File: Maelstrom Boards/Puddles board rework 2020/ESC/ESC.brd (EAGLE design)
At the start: 101.6 x 101.6 mm, 63 parts, among them P5 MALE1PINHEADER, P6 MALE1PINHEADER, P7 MALE1PINHEADER, P8 MALE1PINHEADER

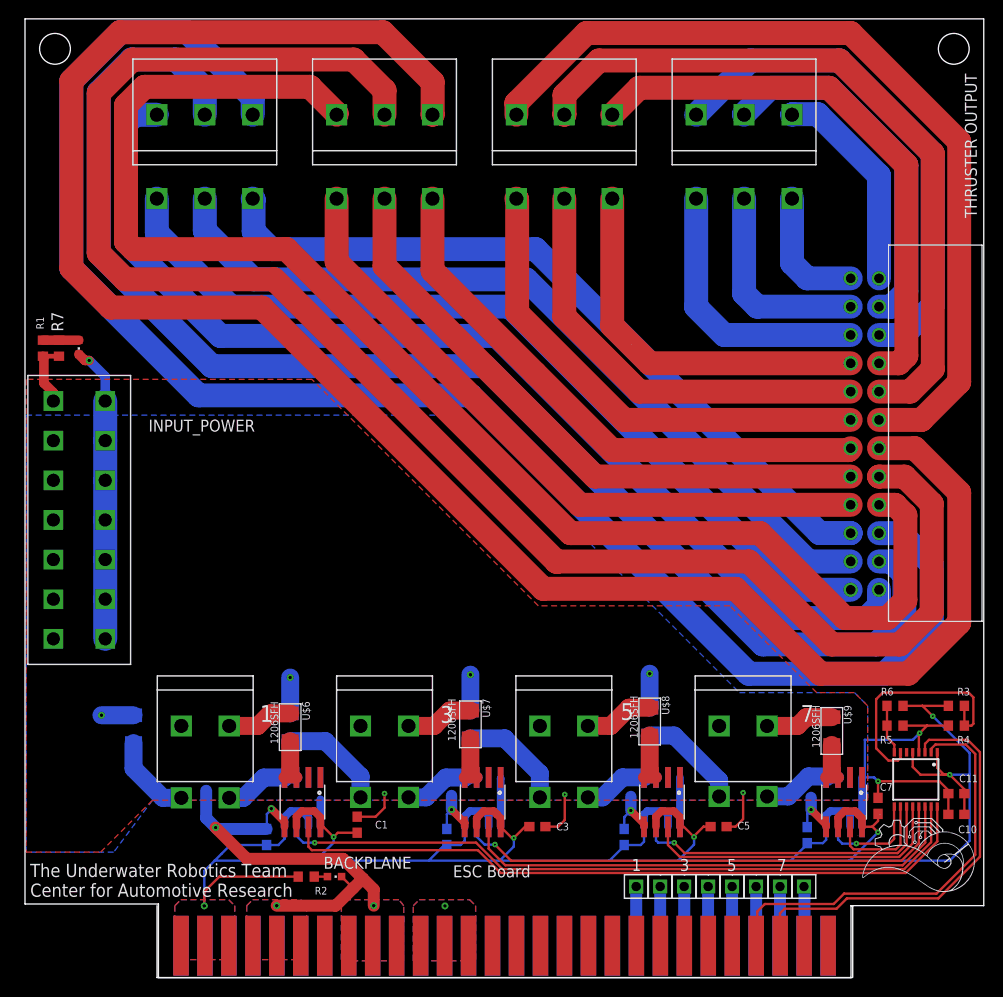
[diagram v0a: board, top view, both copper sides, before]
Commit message: updated puddles board rework ESC and Copro finished
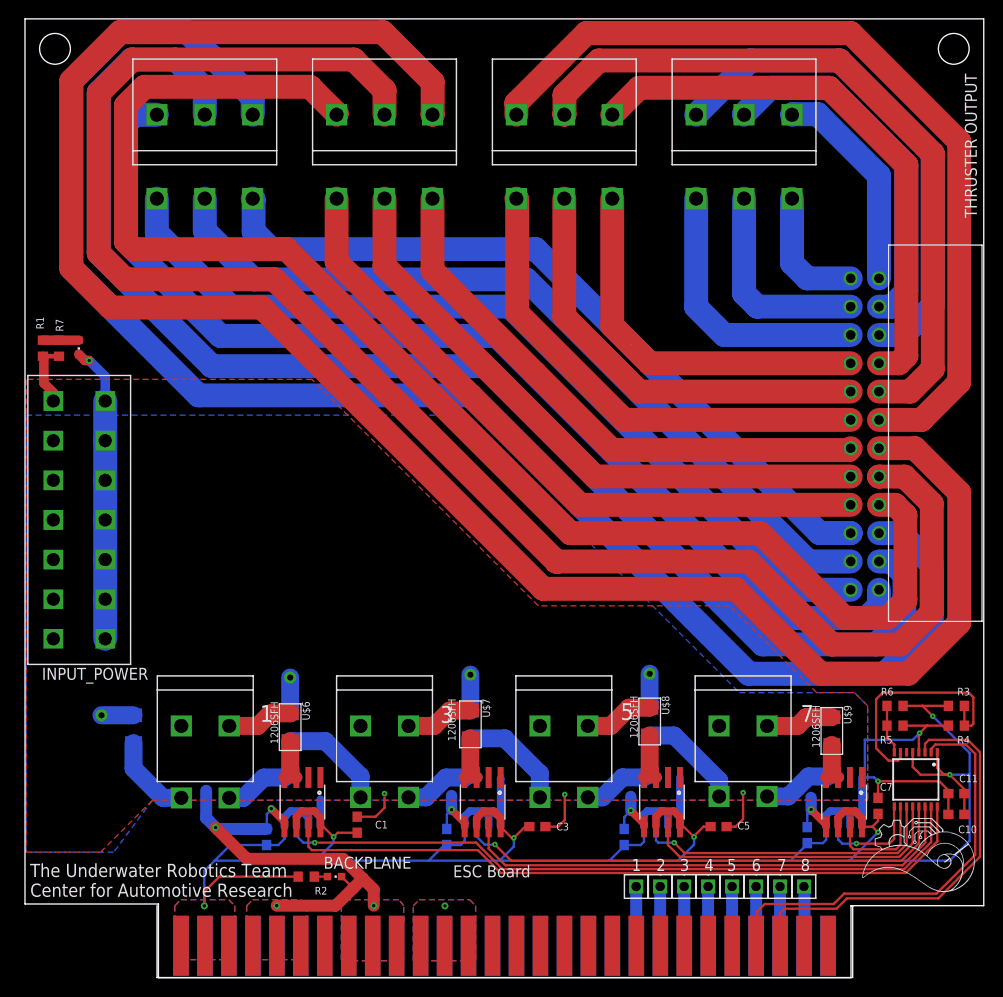
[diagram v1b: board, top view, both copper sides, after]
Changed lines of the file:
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@@
 <text x="2" y="68.7" size="0.8128" layer="25" rot="R90">R1</text>
 <text x="83.2" y="11.3" size="1.27" layer="26" rot="MR0">8</text>
+<text x="66.9" y="11.3" size="1.27" layer="25">2</text>
+<text x="72" y="11.3" size="1.27" layer="25">4</text>
+<text x="77" y="11.3" size="1.27" layer="25">6</text>
+<text x="82.2" y="11.3" size="1.27" layer="25">8</text>
+<text x="65.3" y="11.3" size="1.27" layer="26" rot="MR0">1</text>
+<text x="70.4" y="11.3" size="1.27" layer="26" rot="MR0">3</text>
+<text x="75.4" y="11.3" size="1.27" layer="26" rot="MR0">5</text>
+<text x="80.4" y="11.3" size="1.27" layer="26" rot="MR0">7</text>
 </plain>
 <attributes>
@@
 </element>
 <element name="INPUT_POWER" library="led" library_urn="urn:adsk.eagle:library:259" package="CHIPLED_0603" package3d_urn="urn:adsk.eagle:package:15822/2" value="" x="5.7" y="66.8" smashed="yes" rot="R180">
-<attribute name="NAME" x="24.365" y="59.13" size="1.27" layer="25" rot="R180"/>
+<attribute name="NAME" x="13.065" y="32.83" size="1.27" layer="25" rot="R180"/>
 <attribute name="VALUE" x="3.795" y="68.07" size="1.27" layer="27" rot="R270"/>
 </element>
@@
 </element>
 <element name="R7" library="resistor" library_urn="urn:adsk.eagle:library:348" package="R0603" package3d_urn="urn:adsk.eagle:package:26057/1" value="900" x="3.6" y="66.7" smashed="yes" rot="R90">
-<attribute name="NAME" x="4.065" y="68.465" size="1.27" layer="25" rot="R90"/>
+<attribute name="NAME" x="4.065" y="68.465" size="0.8128" layer="25" rot="R90"/>
 <attribute name="VALUE" x="5.505" y="66.065" size="1.27" layer="27" rot="R90"/>
 </element>
@@
 <contactref element="U$3" pad="P$1"/>
 <wire x1="11.5" y1="27.8" x2="8.1" y2="27.8" width="1.905" layer="16"/>
-<via x="8.1" y="27.8" extent="1-16" drill="0.35"/>
+<via x="8.1" y="27.8" extent="1-16" drill="0.65" diameter="1.3"/>
 <wire x1="28.1" y1="28" x2="28.1" y2="31.8" width="1.905" layer="16"/>
-<via x="28.1" y="31.8" extent="1-16" drill="0.35"/>
+<via x="28.1" y="31.8" extent="1-16" drill="0.65" diameter="1.3"/>
 <wire x1="47.2" y1="28.3" x2="47.2" y2="32.1" width="1.905" layer="16"/>
-<via x="47.2" y="32.1" extent="1-16" drill="0.35"/>
+<via x="47.2" y="32.1" extent="1-16" drill="0.65" diameter="1.3"/>
 <wire x1="66.2" y1="28.6" x2="66.2" y2="32.2" width="1.905" layer="16"/>
-<via x="66.2" y="32.2" extent="1-16" drill="0.35"/>
+<via x="66.2" y="32.2" extent="1-16" drill="0.65" diameter="1.3"/>
 </signal>
 <signal name="PWM_1">

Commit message: Changing puddles values
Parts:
- BACKPLANE: value (none) -> Red
- R1, R7: value 900 -> 2k
- R2: value 5 -> 68
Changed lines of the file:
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@@
 <?xml version="1.0" encoding="utf-8"?>
 <!DOCTYPE eagle SYSTEM "eagle.dtd">
-<eagle version="9.5.2">
+<eagle version="9.6.2">
 <drawing>
 <settings>
@@
 <element name="P8" library="Male_Header_1Pin" package="MALE1PINHEADER" value="MALE1PINHEADER" x="82.55" y="9.652" smashed="yes" rot="R90"/>
 <element name="U$19" library="14_Pin_Connector_Vert" package="14PIN_VERT" value="14PIN_VERT" x="3" y="35.9" smashed="yes"/>
-<element name="R1" library="resistor" library_urn="urn:adsk.eagle:library:348" package="R0603" package3d_urn="urn:adsk.eagle:package:26057/1" value="900" x="1.9" y="66.7" smashed="yes" rot="R90">
+<element name="R1" library="resistor" library_urn="urn:adsk.eagle:library:348" package="R0603" package3d_urn="urn:adsk.eagle:package:26057/1" value="2k" x="1.9" y="66.7" smashed="yes" rot="R90">
 <attribute name="VALUE" x="3.805" y="66.065" size="1.27" layer="27" rot="R90"/>
 </element>
-<element name="R2" library="resistor" library_urn="urn:adsk.eagle:library:348" package="R0603" package3d_urn="urn:adsk.eagle:package:26057/1" value="5" x="29.8" y="10.7" smashed="yes">
+<element name="R2" library="resistor" library_urn="urn:adsk.eagle:library:348" package="R0603" package3d_urn="urn:adsk.eagle:package:26057/1" value="68" x="29.8" y="10.7" smashed="yes">
 <attribute name="VALUE" x="29.165" y="8.795" size="1.27" layer="27"/>
 </element>
-<element name="BACKPLANE" library="led" library_urn="urn:adsk.eagle:library:259" package="CHIPLED_0603" package3d_urn="urn:adsk.eagle:package:15822/2" value="" x="32.8" y="10.7" smashed="yes" rot="R270">
+<element name="BACKPLANE" library="led" library_urn="urn:adsk.eagle:library:259" package="CHIPLED_0603" package3d_urn="urn:adsk.eagle:package:15822/2" value="Red" x="32.8" y="10.7" smashed="yes" rot="R270">
 <attribute name="NAME" x="31.63" y="11.535" size="1.27" layer="25"/>
 <attribute name="VALUE" x="31.53" y="8.795" size="1.27" layer="27"/>
@@
 <attribute name="SPICEPREFIX" value="C" x="98.7" y="19.5" size="1.778" layer="27" display="off"/>
 </element>
-<element name="R7" library="resistor" library_urn="urn:adsk.eagle:library:348" package="R0603" package3d_urn="urn:adsk.eagle:package:26057/1" value="900" x="3.6" y="66.7" smashed="yes" rot="R90">
+<element name="R7" library="resistor" library_urn="urn:adsk.eagle:library:348" package="R0603" package3d_urn="urn:adsk.eagle:package:26057/1" value="2k" x="3.6" y="66.7" smashed="yes" rot="R90">
 <attribute name="NAME" x="4.065" y="68.465" size="0.8128" layer="25" rot="R90"/>
 <attribute name="VALUE" x="5.505" y="66.065" size="1.27" layer="27" rot="R90"/>
